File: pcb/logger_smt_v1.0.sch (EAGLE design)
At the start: 33 parts, among them J1 MICRO-SDCARD-CONNECTOR-330006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, U1 DS1307ZN-1900100P1, U2 CJ1117-3.3-1310190P1, U3 74VHCT125PW, X1 32.768KHZ

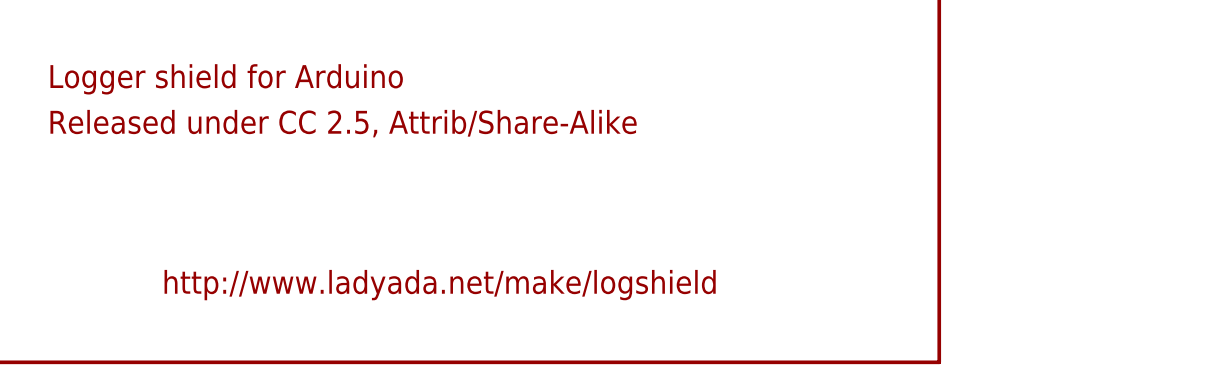
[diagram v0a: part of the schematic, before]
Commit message: Changed attribution and removed adafruit trademark
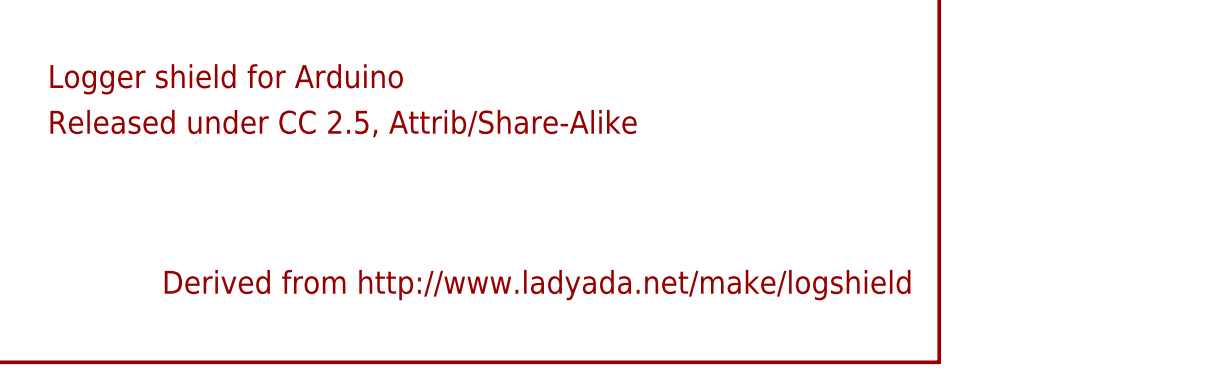
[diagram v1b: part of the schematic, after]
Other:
- note added: "Derived from http://www.ladyada.net/make/logshield"
- note removed: "http://www.ladyada.net/make/logshield"
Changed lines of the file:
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@@
 <sheet>
 <plain>
-<text x="162.56" y="7.62" size="2.54" layer="94">http://www.ladyada.net/make/logshield</text>
+<text x="162.56" y="7.62" size="2.54" layer="94">Derived from http://www.ladyada.net/make/logshield</text>
 <text x="149.86" y="25.4" size="2.54" layer="94">Released under CC 2.5, Attrib/Share-Alike</text>
 <text x="149.86" y="30.48" size="2.54" layer="94">Logger shield for Arduino</text>
